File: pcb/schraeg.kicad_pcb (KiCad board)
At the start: 2 copper layers, 84.5 x 128.5 mm, 103 parts, among them J1 PJ398SM, J2 PJ398SM, J3 PJ398SM, J4 PJ398SM, J5 PJ398SM, J6 PJ398SM, J7 PJ398SM, J8 POWER, SW1 CS12ANW03, SW2 CS12ANW03, SW3 CS12ANW03, U1 TL074, U2 TL074, U3 V2164, U4 TL074, U5 TL074

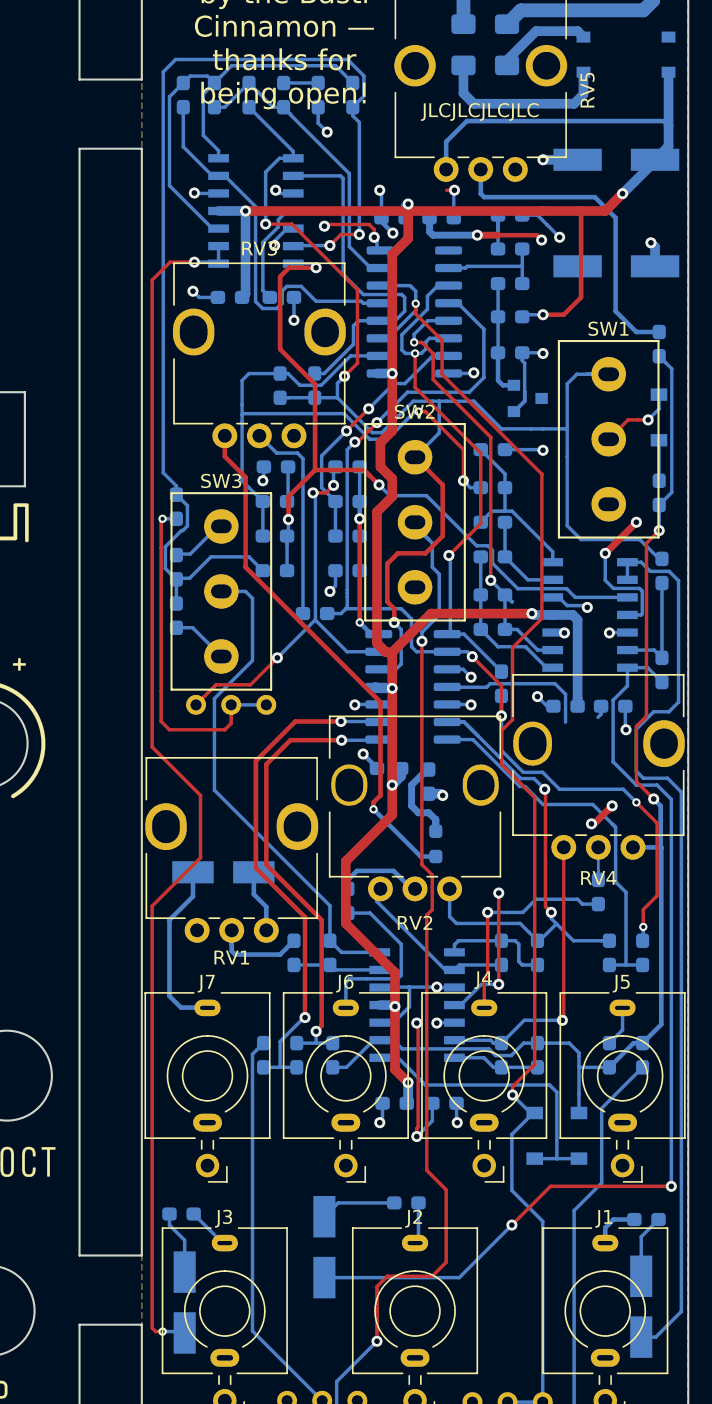
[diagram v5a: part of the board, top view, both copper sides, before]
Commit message: #7 - Removed the -5V reference. Changed R12 to have the same effect as before with -12V (-10.8V after the rectifier).
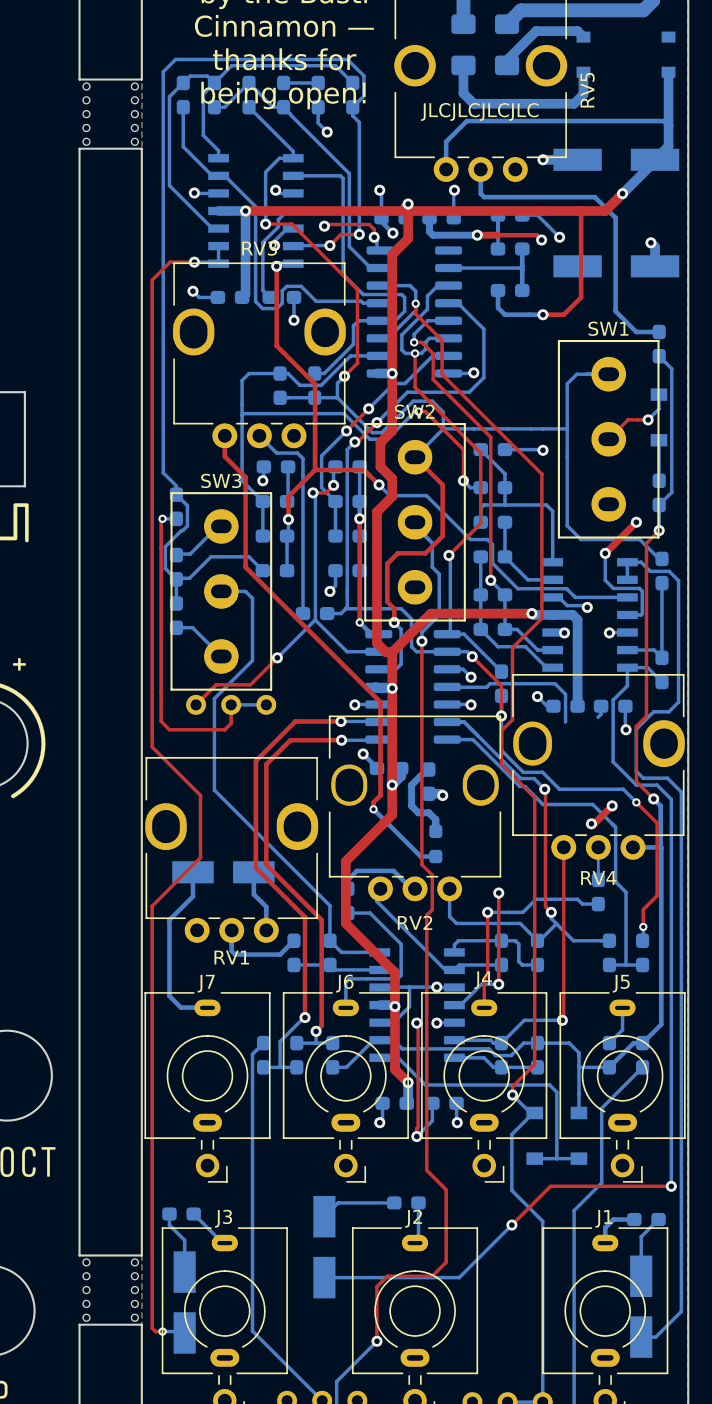
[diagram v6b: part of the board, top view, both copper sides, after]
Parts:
- removed C18: 220n, Capacitor_SMD:C_0603_1608Metric_Pad1.05x0.95mm_HandSolder
- removed D6: LM4040DBZ-5, Package_TO_SOT_SMD:SOT-23
- removed R47: 6K8, Resistor_SMD:R_0603_1608Metric_Pad1.05x0.95mm_HandSolder
- added REF**: MountingHole_2.1mm, MountingHole:MountingHole_2.1mm, F.Cu at (44.5, 110.5)
- added REF**: MountingHole_2.1mm, MountingHole:MountingHole_2.1mm, F.Cu at (44.5, 21.5)
- added REF**: MountingHole_2.1mm, MountingHole:MountingHole_2.1mm, F.Cu at (41.0, 110.5)
- added REF**: MountingHole_2.1mm, MountingHole:MountingHole_2.1mm, F.Cu at (41.0, 109.5)
- added REF**: MountingHole_2.1mm, MountingHole:MountingHole_2.1mm, F.Cu at (41.0, 108.5)
- added REF**: MountingHole_2.1mm, MountingHole:MountingHole_2.1mm, F.Cu at (41.0, 107.5)
- added REF**: MountingHole_2.1mm, MountingHole:MountingHole_2.1mm, F.Cu at (41.0, 106.5)
- added REF**: MountingHole_2.1mm, MountingHole:MountingHole_2.1mm, F.Cu at (41.0, 25.5)
- added REF**: MountingHole_2.1mm, MountingHole:MountingHole_2.1mm, F.Cu at (41.0, 24.5)
- added REF**: MountingHole_2.1mm, MountingHole:MountingHole_2.1mm, F.Cu at (41.0, 23.5)
- added REF**: MountingHole_2.1mm, MountingHole:MountingHole_2.1mm, F.Cu at (41.0, 22.5)
- added REF**: MountingHole_2.1mm, MountingHole:MountingHole_2.1mm, F.Cu at (44.5, 109.5)
- added REF**: MountingHole_2.1mm, MountingHole:MountingHole_2.1mm, F.Cu at (41.0, 21.5)
- added REF**: MountingHole_2.1mm, MountingHole:MountingHole_2.1mm, F.Cu at (44.5, 108.5)
- added REF**: MountingHole_2.1mm, MountingHole:MountingHole_2.1mm, F.Cu at (44.5, 107.5)
- added REF**: MountingHole_2.1mm, MountingHole:MountingHole_2.1mm, F.Cu at (44.5, 106.5)
- added REF**: MountingHole_2.1mm, MountingHole:MountingHole_2.1mm, F.Cu at (44.5, 25.5)
- added REF**: MountingHole_2.1mm, MountingHole:MountingHole_2.1mm, F.Cu at (44.5, 24.5)
- added REF**: MountingHole_2.1mm, MountingHole:MountingHole_2.1mm, F.Cu at (44.5, 23.5)
- added REF**: MountingHole_2.1mm, MountingHole:MountingHole_2.1mm, F.Cu at (44.5, 22.5)
- R12: value 100K -> 220K
- moved R12 0.50 mm to (71.6, 36.2)
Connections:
- R12 pad 2: -5V_REF -> -12V
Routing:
- net GND: track 69.2 -> 60.8 mm, vias 31 -> 30
- net -5V_REF: track 8.29 -> 0.00 mm
- net -12V: track 173.7 -> 176.8 mm
- net HP_OUT: track 54.7 -> 52.5 mm
- net Net-(R36-Pad1): track 12.7 -> 14.9 mm
- net Net-(R12-Pad1): track 7.65 -> 9.63 mm
- net Net-(C9-Pad2): track 32.8 -> 31.3 mm
- net BP_OUT: track 100.3 -> 99.1 mm

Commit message: New pcb distribution
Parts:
- removed G***: LOGO, schraeg:silkF
- removed the REF** at (44.5, 110.5)
- removed the REF** at (44.5, 21.5)
- removed the REF** at (41.0, 110.5)
- removed the REF** at (41.0, 109.5)
- removed the REF** at (41.0, 108.5)
- removed the REF** at (41.0, 107.5)
- removed the REF** at (41.0, 106.5)
- removed the REF** at (41.0, 25.5)
- removed the REF** at (41.0, 24.5)
- removed the REF** at (41.0, 23.5)
- removed the REF** at (41.0, 22.5)
- removed the REF** at (44.5, 109.5)
- removed the REF** at (41.0, 21.5)
- removed the REF** at (44.5, 108.5)
- removed the REF** at (44.5, 107.5)
- removed the REF** at (44.5, 106.5)
- removed the REF** at (44.5, 25.5)
- removed the REF** at (44.5, 24.5)
- removed the REF** at (44.5, 23.5)
- removed the REF** at (44.5, 22.5)
- added REF**: LED_D5.0mm, LED_THT:LED_D5.0mm, F.Cu at (114.0, 131.5)
- C1, C10, C11, C12, C13, C19, C20, C21, C22, C23, C24, C25, C26, C27, C28, C3, C7, C8, C9: footprint Capacitor_SMD:C_0603_1608Metric_Pad1.05x0.95mm_HandSolder -> Capacitor_SMD:C_0603_1608Metric_Pad1.08x0.95mm_HandSolder
- R1, R10, R12, R13, R14, R15, R16, R17, R18, R19, R2, R20, R21, R22, R23, R24, R25, R26, R27, R28, R29, R3, R30, R31, R32, R33, R34, R35, R36, R37, R38, R39, R4, R40, R41, R42, R43, R48, R49, R5, R6, R7, R9: footprint Resistor_SMD:R_0603_1608Metric_Pad1.05x0.95mm_HandSolder -> Resistor_SMD:R_0603_1608Metric_Pad0.98x0.95mm_HandSolder
- U1, U2, U4, U5: footprint Package_SO:SOIC-14_3.9x8.7mm_P1.27mm -> Package_SO:TSSOP-14_4.4x5mm_P0.65mm
- moved C6 195.2 mm to (243.3, 110.0), turned to 0 degrees
- moved C2 193.6 mm to (240.6, 116.9)
- moved C5 162.8 mm to (219.4, 82.6), turned to 0 degrees
- moved R25 154.7 mm to (196.9, 61.5), turned to 0 degrees
- moved C4 150.5 mm to (230.0, 87.9), turned to 0 degrees
- moved R22 145.0 mm to (192.5, 59.0), turned to 0 degrees
- moved R43 144.3 mm to (192.5, 46.4), turned to 0 degrees
- moved R39 139.9 mm to (192.5, 48.9), turned to 0 degrees
- moved R28 137.9 mm to (192.5, 56.5), turned to 0 degrees
- moved R38 137.6 mm to (188.2, 46.4), turned to 0 degrees
- moved R49 137.5 mm to (192.5, 43.9), turned to 0 degrees
- moved R30 137.1 mm to (196.9, 59.0), turned to 0 degrees
- moved R26 136.4 mm to (183.8, 48.9), turned to 0 degrees
- moved R34 136.1 mm to (192.5, 54.0), turned to 0 degrees
- moved R17 135.0 mm to (192.5, 61.5), turned to 0 degrees
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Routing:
- net -12V: track 176.8 -> 0.00 mm, vias 10 -> 0
- net Net-(D1-Pad2): track 100.4 -> 0.00 mm, vias 2 -> 0
- net BP_OUT: track 99.1 -> 0.00 mm, vias 3 -> 0
- net FREQ_CV: track 98.6 -> 0.00 mm, vias 2 -> 0
- net Net-(C6-Pad1): track 87.8 -> 0.00 mm, vias 2 -> 0
- net AUDIO_IN: track 80.0 -> 0.00 mm, vias 2 -> 0
- net Net-(RV6-Pad1): track 77.2 -> 0.00 mm, vias 2 -> 0
- net +12V: track 75.8 -> 0.00 mm, vias 12 -> 0
- net Net-(C3-Pad2): track 75.2 -> 0.00 mm, vias 6 -> 0
- net Net-(C5-Pad1): track 71.3 -> 0.00 mm, vias 2 -> 0
- net Net-(C4-Pad1): track 66.3 -> 0.00 mm
- net GND: track 60.8 -> 0.00 mm, vias 30 -> 0
- net HP_OUT: track 52.5 -> 0.00 mm, vias 3 -> 0
- net Net-(C10-Pad2): track 45.5 -> 0.00 mm, vias 2 -> 0
- net RES_CV: track 39.0 -> 0.00 mm, vias 2 -> 0
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- removed copper zone on B.Cu, net +12V
- removed copper zone on F.Cu, net GND
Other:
- board size 84.5 x 128.5 mm -> 39.5 x 110 mm
- rule pad_to_mask_clearance: 0.051 -> 0
- board text removed: "JLCJLCJLCJLC"
- board text removed: "Power Either Way"
- board text removed: "Res. Adj."
- board text removed: "Rework by F1N05"
- board text removed: "Saw Adj."
- board text removed: "Schräg inspired by the Bastl Cinnamon — thanks for being open!"
- board text removed: "Schräg v0.2.2 Barnaby Walters waterpigs.co.uk cc-by-sa 2021"
- board text removed: "V/oct Adj."

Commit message: PCB Layout finished.
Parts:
- removed REF**: LED_D5.0mm, LED_THT:LED_D5.0mm
- D3: footprint Diode_SMD:D_SOD-123 -> Diode_SMD:D_SOT-23_ANK
- RV6, RV7, RV8: footprint Potentiometer_THT:Potentiometer_Bourns_3296W_Vertical -> Potentiometer_THT:Potentiometer_Bourns_3266Y_Vertical
- moved C6 137.2 mm to (106.8, 122.8), turned to 270 degrees
- moved C2 136.8 mm to (105.8, 140.0)
- moved R25 133.7 mm to (102.0, 155.8), turned to 90 degrees
- moved R49 118.3 mm to (114.8, 133.0), turned to 270 degrees
- moved R23 117.0 mm to (136.5, 158.5)
- moved R9 116.7 mm to (111.5, 146.8), turned to 270 degrees
- moved C4 116.5 mm to (134.5, 154.5)
- moved R10 116.4 mm to (109.2, 146.8), turned to 270 degrees
- moved R14 112.1 mm to (117.2, 145.8), turned to 90 degrees
- moved R18 110.8 mm to (106.8, 132.5), turned to 90 degrees
- moved R19 109.8 mm to (112.0, 137.0), turned to 270 degrees
- moved R5 106.8 mm to (119.8, 142.8)
- moved R48 105.0 mm to (127.5, 127.8), turned to 90 degrees
- moved R3 101.1 mm to (127.5, 137.2), turned to 270 degrees
- moved R2 100.3 mm to (127.0, 142.0), turned to 90 degrees
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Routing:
- net -12V: track 0.00 -> 179.4 mm, vias 0 -> 11
- net +12V: track 0.00 -> 145.1 mm, vias 0 -> 11
- net FREQ_CV: track 0.00 -> 109.6 mm, vias 0 -> 5
- net Net-(R19-Pad1): track 0.00 -> 107.8 mm, vias 0 -> 1
- net BP_OUT: track 0.00 -> 97.6 mm, vias 0 -> 1
- net Net-(D1-Pad2): track 0.00 -> 87.0 mm, vias 0 -> 2
- net Net-(R10-Pad2): track 0.00 -> 77.2 mm, vias 0 -> 1
- net Net-(C3-Pad2): track 0.00 -> 73.9 mm, vias 0 -> 3
- net Net-(C4-Pad1): track 0.00 -> 73.2 mm, vias 0 -> 2
- net AUDIO_IN: track 0.00 -> 58.7 mm, vias 0 -> 4
- net HP_OUT: track 0.00 -> 57.1 mm, vias 0 -> 2
- net Net-(C6-Pad1): track 0.00 -> 48.6 mm
- net Net-(J2-PadT): track 0.00 -> 47.4 mm
- net Net-(R13-Pad1): track 0.00 -> 45.1 mm, vias 0 -> 2
- net Net-(J5-PadT): track 0.00 -> 44.8 mm, vias 0 -> 1
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- added copper zone on B.Cu, net GND
- added copper zone on F.Cu, net GND
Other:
- outline, holes or cut-outs redrawn
